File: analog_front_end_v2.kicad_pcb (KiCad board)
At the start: 4 copper layers, 155 parts, among them J1 Conn_Coaxial, J3 Conn_01x01_Socket, J4 Conn_01x01_Socket, U1 ADL5531, U10 PMOD 2x6, U11 LP2985-5.0, U12 LP2985-5.0, U13 LT1363, U14 MAX 735, U15 LP2985-2.5, U16 MAX889SESA, U17 MAX6102, U2 ADL5531, U3 ADL5531, U4 PE4140B-Z, U5 ADF4360-9, U6 LTC1406, U7 THS4551, U8 LT1363, U9 PMOD 2x6

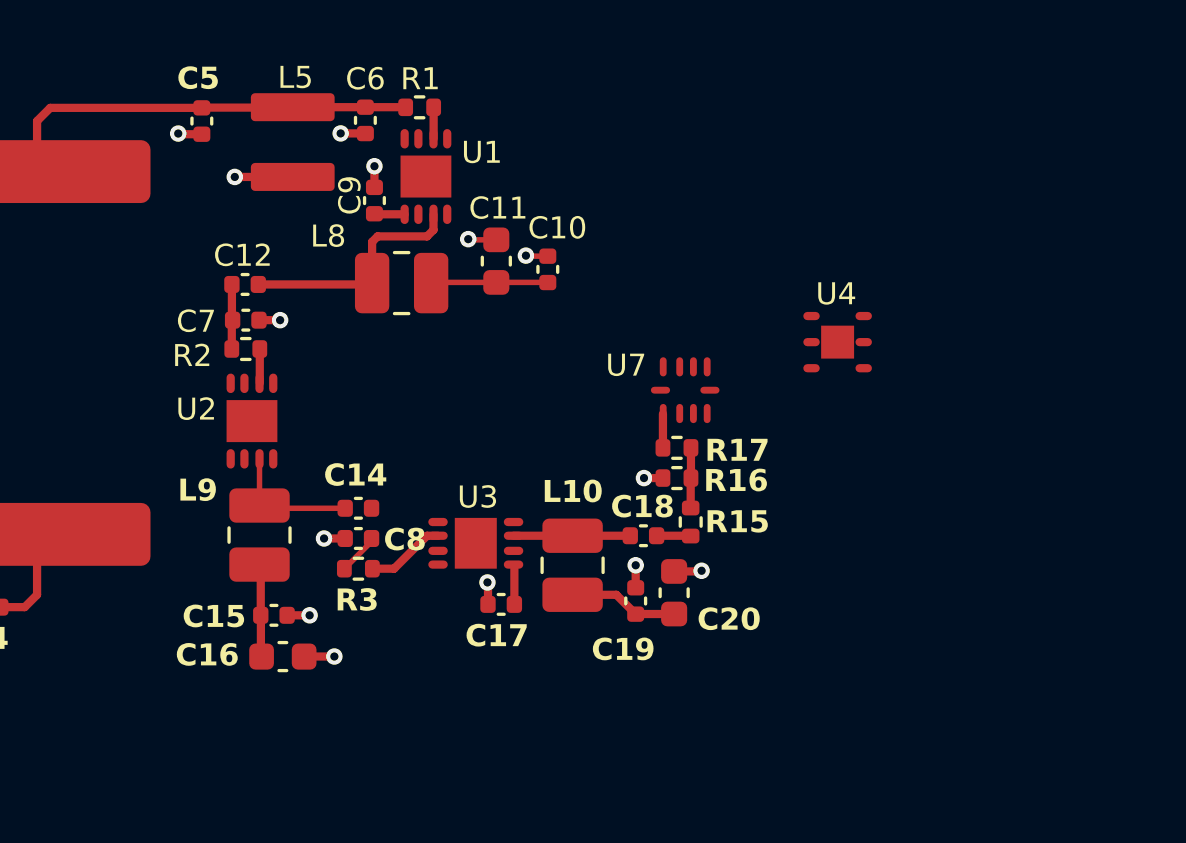
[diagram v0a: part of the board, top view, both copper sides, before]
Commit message: Shrunk RF amp section
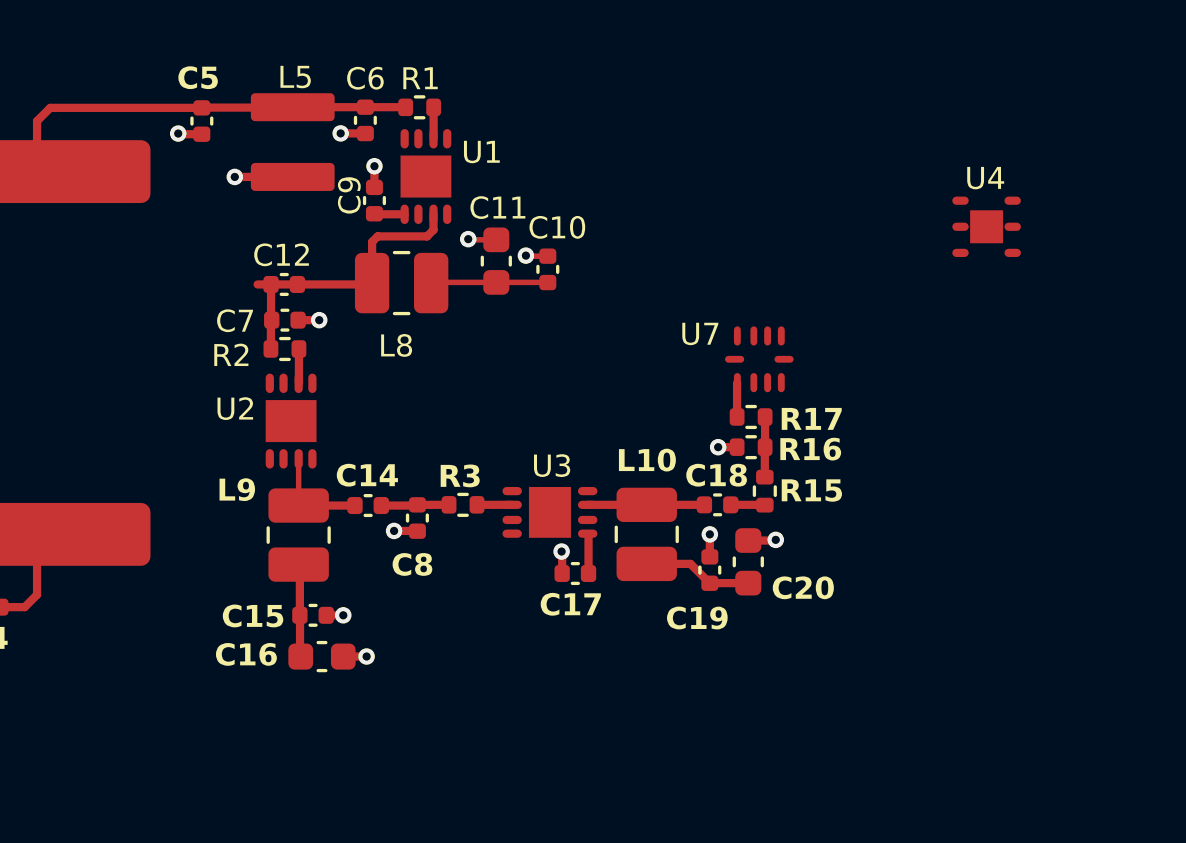
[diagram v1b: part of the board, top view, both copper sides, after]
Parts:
- moved U4 6.86 mm to (93.8, 22.1)
- moved R3 4.46 mm to (74.7, 32.3)
- moved C17 2.93 mm to (78.8, 34.8)
- moved C18 2.93 mm to (84.0, 32.3)
- moved C19 2.93 mm to (83.7, 34.6)
- moved C20 2.93 mm to (85.1, 34.4)
- moved L10 2.93 mm to (81.4, 33.4)
- moved R15 2.93 mm to (85.7, 31.8)
- moved R16 2.93 mm to (85.2, 30.2)
- moved R17 2.93 mm to (85.2, 29.1)
- moved U3 2.93 mm to (77.9, 32.5)
- moved U7 2.93 mm to (85.5, 27.0)
- moved C8 2.28 mm to (73.0, 32.8), turned to -90 degrees
- moved C12 1.42 mm to (68.2, 24.2)
- moved C15 1.42 mm to (69.2, 36.3)
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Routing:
- net Net-(U3-RFIN): track 2.89 -> 1.28 mm
- net Net-(U2-RFOUT): track 4.86 -> 3.89 mm
- net Net-(C14-Pad2): track 1.51 -> 2.40 mm

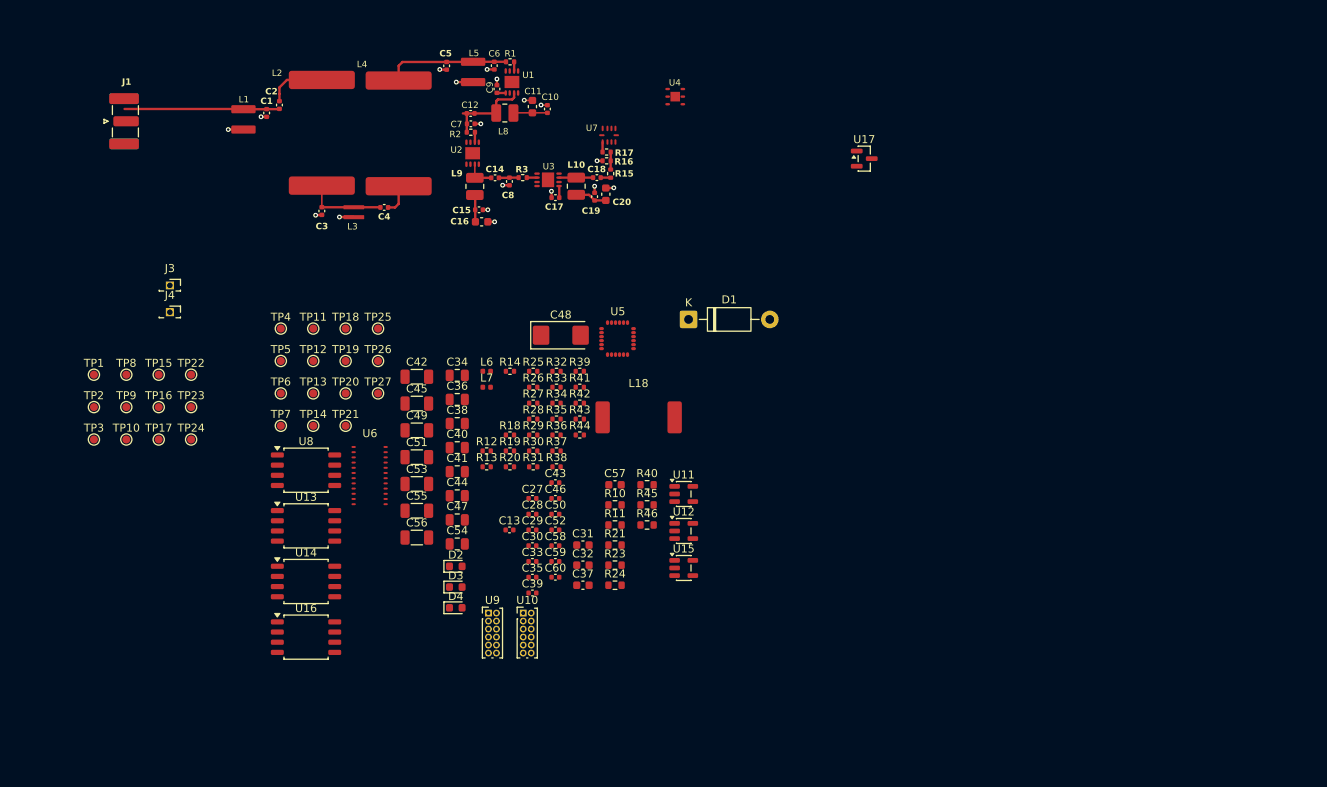
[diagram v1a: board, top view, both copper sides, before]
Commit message: Updated PCB layout with further size reductions around the amplifier stages
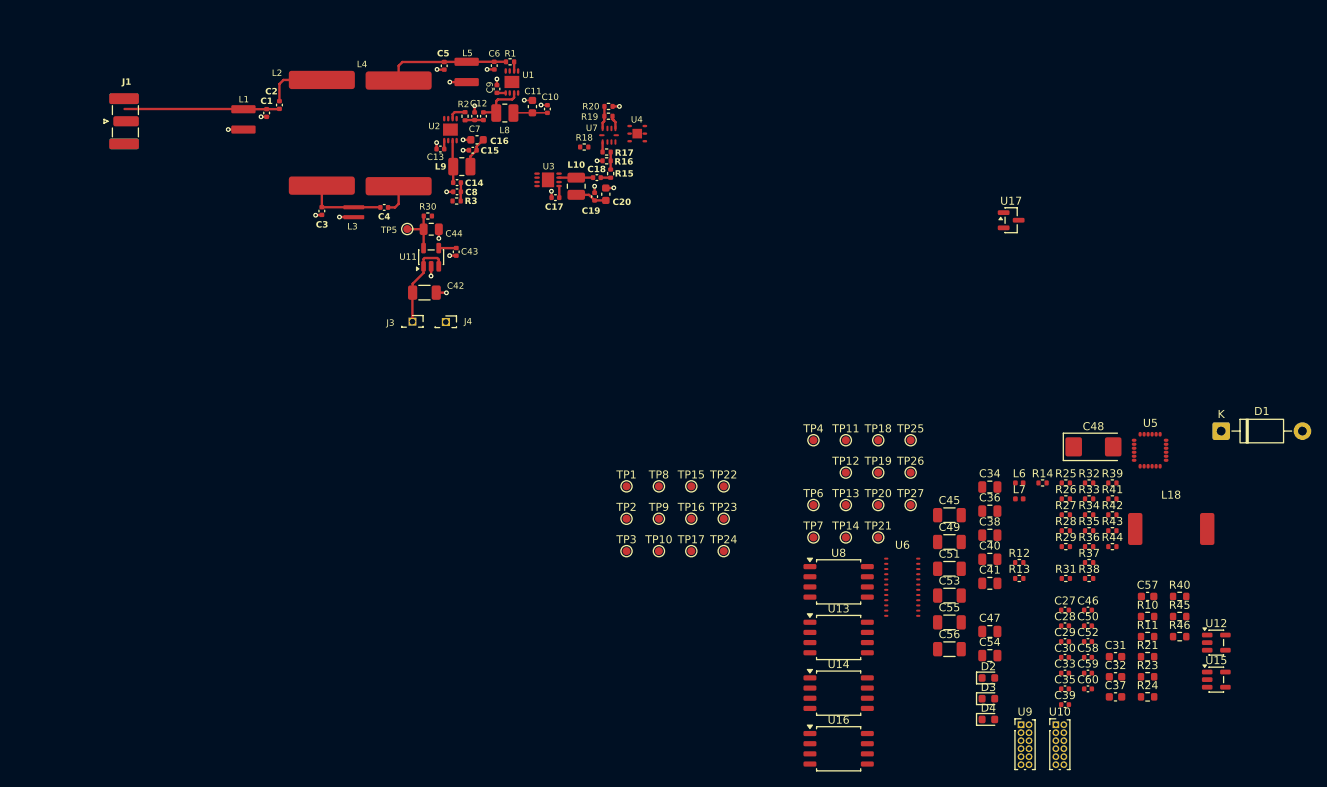
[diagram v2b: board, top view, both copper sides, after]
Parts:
- moved C45 68.0 mm to (128.1, 74.5)
- moved C48 68.0 mm to (146.1, 65.9)
- moved C49 68.0 mm to (128.1, 77.8)
- moved C51 68.0 mm to (128.1, 81.2)
- moved C53 68.0 mm to (128.1, 84.5)
- moved C55 68.0 mm to (128.1, 87.9)
- moved C56 68.0 mm to (128.1, 91.2)
- moved R40 68.0 mm to (156.8, 84.6)
- moved R45 68.0 mm to (156.8, 87.1)
- moved R46 68.0 mm to (156.8, 89.7)
- moved C27 68.0 mm to (142.5, 86.3)
- moved C28 68.0 mm to (142.5, 88.3)
- moved C29 68.0 mm to (142.5, 90.3)
- moved C30 68.0 mm to (142.5, 92.2)
- moved C31 68.0 mm to (148.8, 92.2)
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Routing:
- net VIN: track 0.00 -> 11.3 mm
- net GND: track 18.3 -> 24.7 mm, vias 18 -> 24
- net Net-(U11-VOUT): track 0.00 -> 6.03 mm
- net Net-(U7-IN+): track 0.00 -> 2.84 mm
- net Net-(U11-BP): track 0.00 -> 2.72 mm
- net Net-(U1-RFOUT): track 8.68 -> 6.19 mm
- net DIFF_OUTN: track 0.00 -> 1.69 mm
- net Net-(U2-RFOUT): track 3.89 -> 5.28 mm
- net Net-(U3-RFIN): track 1.28 -> 0.00 mm
- net Net-(U2-CLIN): track 0.00 -> 1.05 mm
- net Net-(U2-RFIN): track 1.25 -> 2.21 mm
- net 5V_LNA: track 12.0 -> 12.6 mm

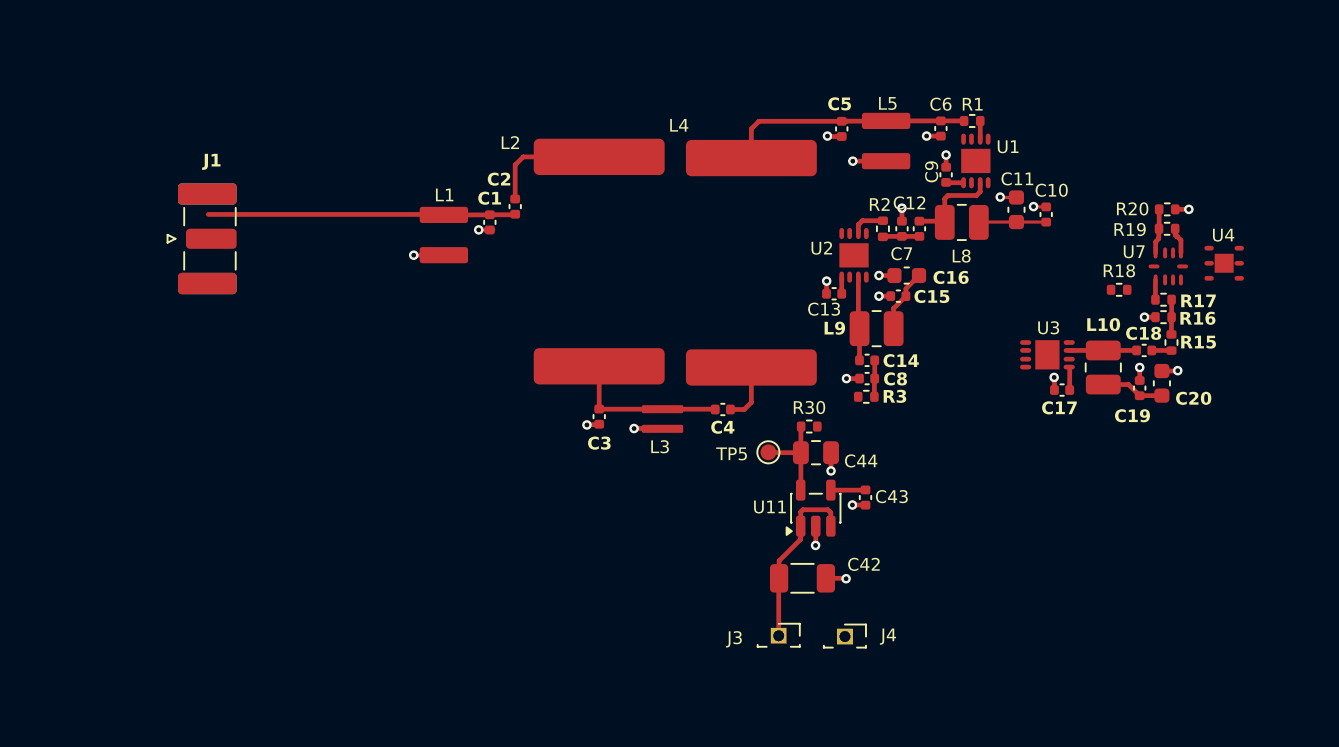
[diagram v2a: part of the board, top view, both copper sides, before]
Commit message: Make the band pass filtering and amps more compact
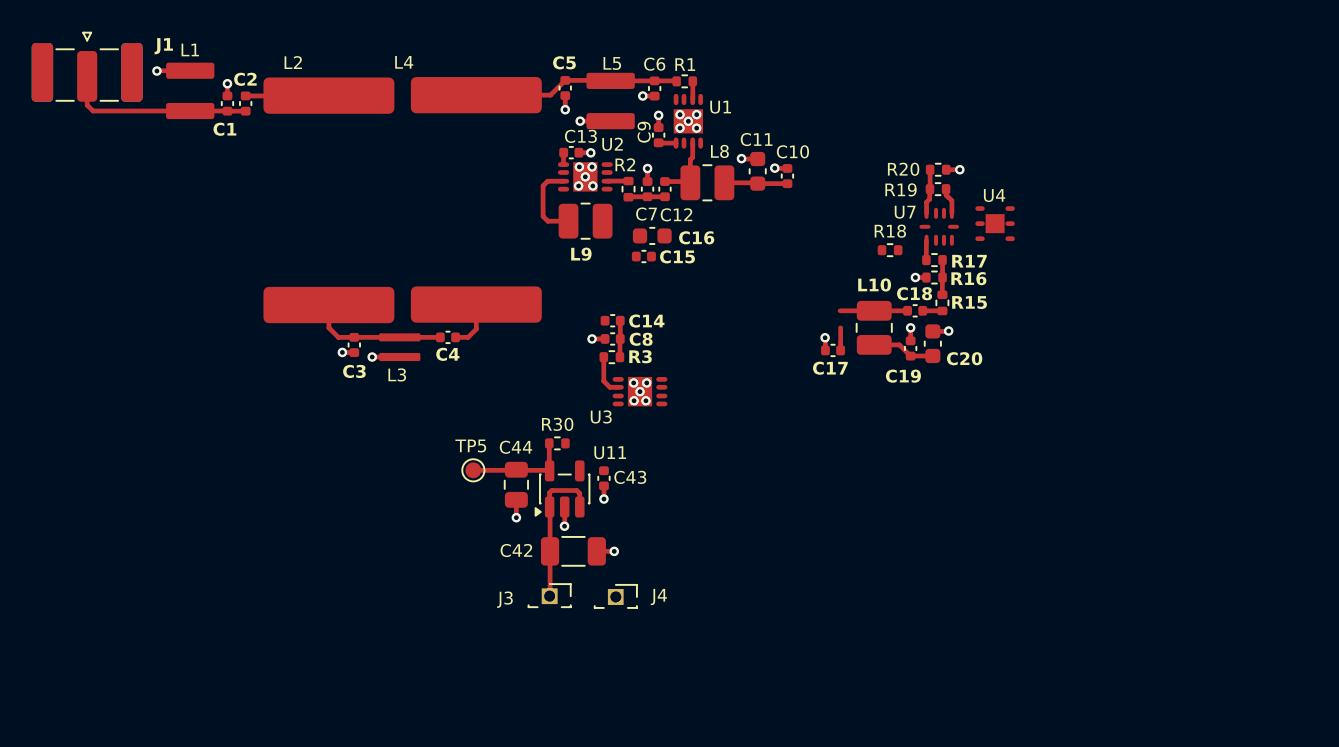
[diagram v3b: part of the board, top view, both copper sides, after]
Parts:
- moved U3 25.8 mm to (52.2, 34.9)
- moved L9 19.6 mm to (48.7, 24.1)
- moved C44 19.0 mm to (44.4, 40.8), turned to 90 degrees
- moved C13 18.8 mm to (47.8, 19.8), turned to 0 degrees
- moved TP5 18.6 mm to (41.7, 39.8)
- moved L1 18.4 mm to (23.8, 15.9), turned to 90 degrees
- moved C9 18.3 mm to (53.4, 18.7)
- moved R1 18.3 mm to (55.0, 15.3)
- moved U1 18.3 mm to (55.2, 17.8)
- moved C6 18.2 mm to (53.1, 15.8)
- moved C2 18.2 mm to (27.3, 16.7)
- moved C1 18.2 mm to (26.1, 16.7), turned to 90 degrees
- moved C4 17.9 mm to (40.1, 31.4)
- moved L4 17.8 mm to (41.9, 22.8)
- moved U2 17.7 mm to (48.7, 21.3), turned to 180 degrees
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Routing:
- net Net-(J1-In): track 19.4 -> 12.0 mm
- net 5V_LNA: track 12.6 -> 8.33 mm
- net Net-(U11-BP): track 2.72 -> 0.00 mm
- net Net-(U3-RFIN): track 0.00 -> 2.58 mm
- net Net-(C2-Pad1): track 7.66 -> 5.26 mm
- net GND: track 24.7 -> 22.4 mm, vias 24 -> 37
- net Net-(U1-RFOUT): track 6.19 -> 4.27 mm
- net VIN: track 11.3 -> 9.47 mm
- net Net-(C3-Pad1): track 10.0 -> 8.72 mm
- net Net-(U2-RFIN): track 2.21 -> 1.35 mm
- net Net-(C4-Pad2): track 3.71 -> 3.08 mm
- net Net-(U11-VOUT): track 6.03 -> 6.59 mm
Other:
- board text added: "TODO: Should pin 7 be connected??"

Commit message: Latest PCB Artwork changes
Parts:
- moved C32 111.6 mm to (61.0, 25.7), turned to 180 degrees
- moved C31 107.5 mm to (59.5, 32.5)
- moved C33 105.9 mm to (60.7, 27.0), turned to 180 degrees
- moved C30 102.9 mm to (59.8, 31.1)
- moved R11 101.3 mm to (68.8, 33.0)
- moved R23 94.7 mm to (81.3, 32.5)
- moved R24 94.7 mm to (81.3, 35.0)
- moved R38 93.3 mm to (68.7, 29.4)
- moved R40 90.3 mm to (79.3, 38.3)
- moved R10 89.1 mm to (75.7, 42.6)
- moved U5 89.0 mm to (68.8, 38.1)
- moved R25 85.6 mm to (69.0, 26.7), turned to 90 degrees
- moved R27 84.5 mm to (74.7, 24.2)
- moved R14 82.2 mm to (63.2, 40.2)
- moved R39 72.3 mm to (82.1, 41.9)
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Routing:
- net Net-(U8--IN): track 0.00 -> 7.24 mm
- net 5V_LNA: track 8.33 -> 15.0 mm
- net Net-(U8-VOUT): track 0.00 -> 6.46 mm
- net GND: track 22.4 -> 27.0 mm, vias 37 -> 44
- net Net-(U2-RFOUT): track 5.07 -> 9.43 mm
- net -5V_OPAMP: track 0.00 -> 4.29 mm
- net Net-(U1-RFOUT): track 4.27 -> 7.05 mm
- net -2.5V_DiffAmp: track 0.00 -> 2.48 mm
- net 2.5V_DiffAmp: track 0.00 -> 2.45 mm
- net Net-(C5-Pad1): track 15.1 -> 17.0 mm
- net DIFF_OUTP: track 0.00 -> 1.67 mm
- net Net-(U3-RFOUT): track 4.25 -> 5.89 mm
- net DIFF_IN-: track 1.25 -> 2.40 mm
- net Net-(U3-CLIN): track 1.46 -> 0.95 mm
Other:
- board text removed: "TODO: Should pin 7 be connected??"

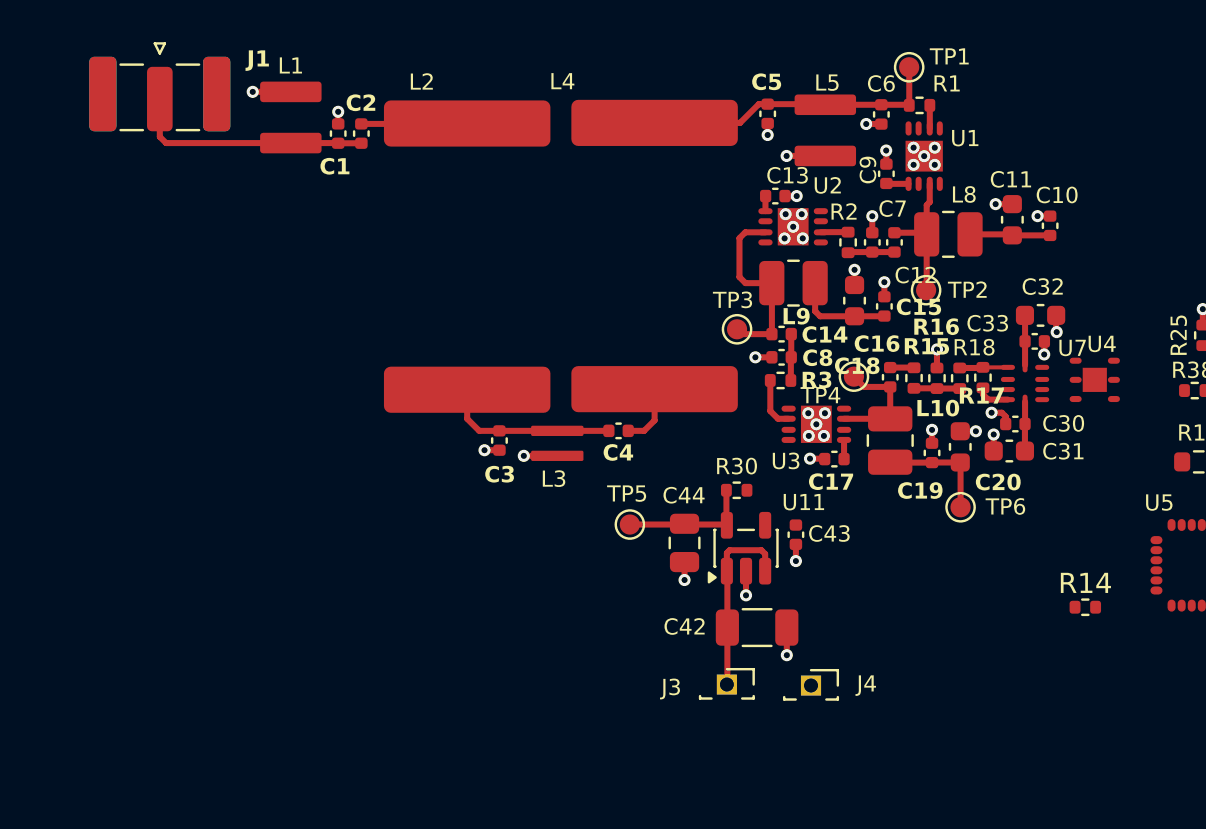
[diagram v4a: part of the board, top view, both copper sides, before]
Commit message: Make RF frontend super compact
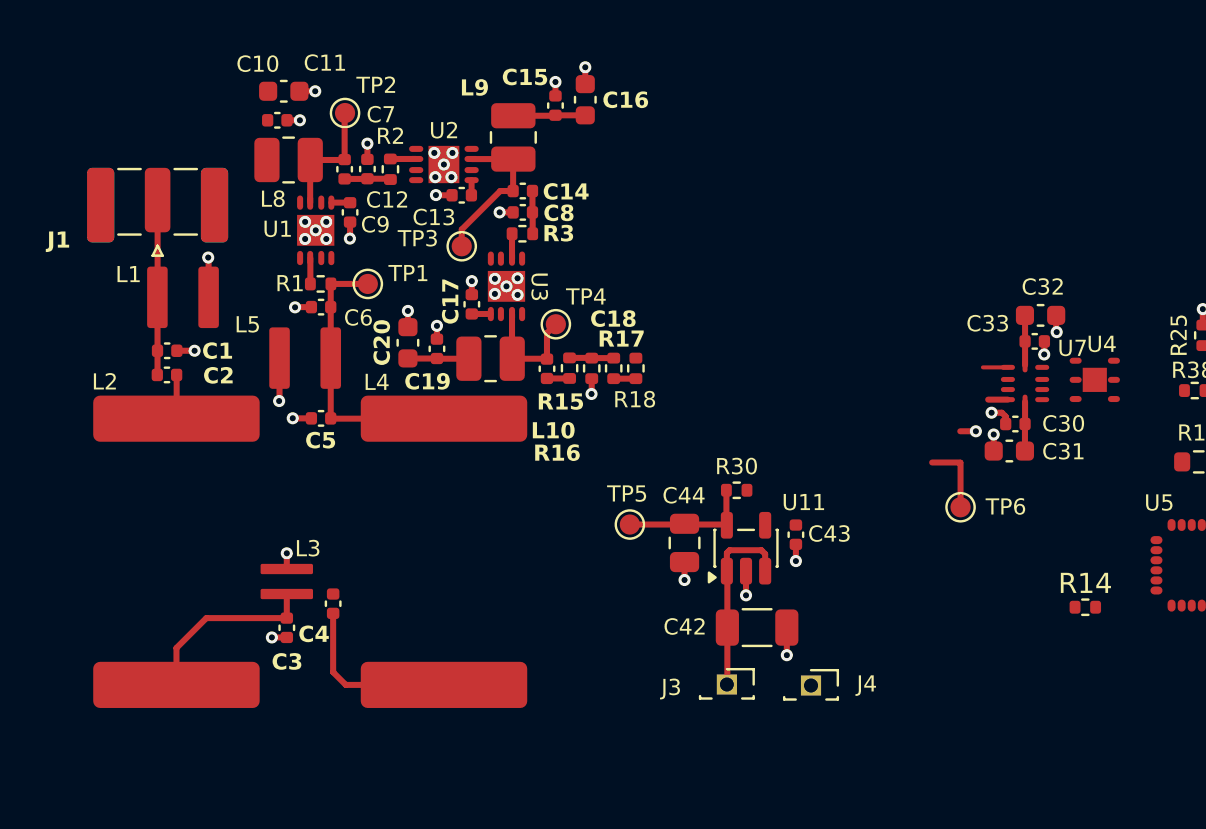
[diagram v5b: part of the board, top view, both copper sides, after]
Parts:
- moved C10 38.7 mm to (23.1, 16.0), turned to 0 degrees
- moved C11 36.7 mm to (23.4, 14.6), turned to 0 degrees
- moved L8 32.9 mm to (23.7, 18.0), turned to 180 degrees
- moved R1 31.0 mm to (25.3, 24.2), turned to 180 degrees
- moved U1 30.4 mm to (25.0, 21.5), turned to 90 degrees
- moved TP2 30.1 mm to (26.5, 15.7)
- moved C6 29.4 mm to (25.3, 25.3), turned to 180 degrees
- moved TP1 28.9 mm to (27.6, 24.2)
- moved L5 28.2 mm to (24.5, 27.8), turned to 180 degrees
- moved C20 27.9 mm to (29.6, 27.1)
- moved C12 27.5 mm to (26.5, 18.5)
- moved C5 26.8 mm to (25.3, 30.8), turned to 180 degrees
- moved C9 26.7 mm to (26.7, 20.6), turned to -90 degrees
- moved C7 25.3 mm to (27.6, 18.5)
- moved C19 25.1 mm to (31.1, 27.4)
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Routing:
- net Net-(C4-Pad2): track 3.08 -> 8.68 mm
- net 5V_LNA: track 15.0 -> 10.2 mm
- net Net-(J1-In): track 12.0 -> 8.69 mm
- net Net-(C2-Pad1): track 5.26 -> 2.17 mm
- net Net-(C5-Pad1): track 17.0 -> 14.2 mm
- net Net-(U2-RFOUT): track 9.43 -> 7.83 mm
- net Net-(U3-RFIN): track 2.58 -> 1.24 mm
- net Net-(U1-RFOUT): track 7.05 -> 6.15 mm
- net DIFF_OUTP: track 1.67 -> 1.02 mm
- net GND: track 27.0 -> 27.6 mm, vias 44 -> 45
